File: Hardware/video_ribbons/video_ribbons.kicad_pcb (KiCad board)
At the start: 4 copper layers, 124.5 x 99.1 mm, 82 parts, among them J1 Conn_Coaxial_Sleeve_Pin2Tip, J2 Conn_01x02, J5 Conn_02x08_Odd_Even, J6 Conn_02x04_Odd_Even, J7 Conn_02x08_Odd_Even, U1 74HC138, U10 74HC161, U11 74HC161, U12 74HC30, U13 74HC08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

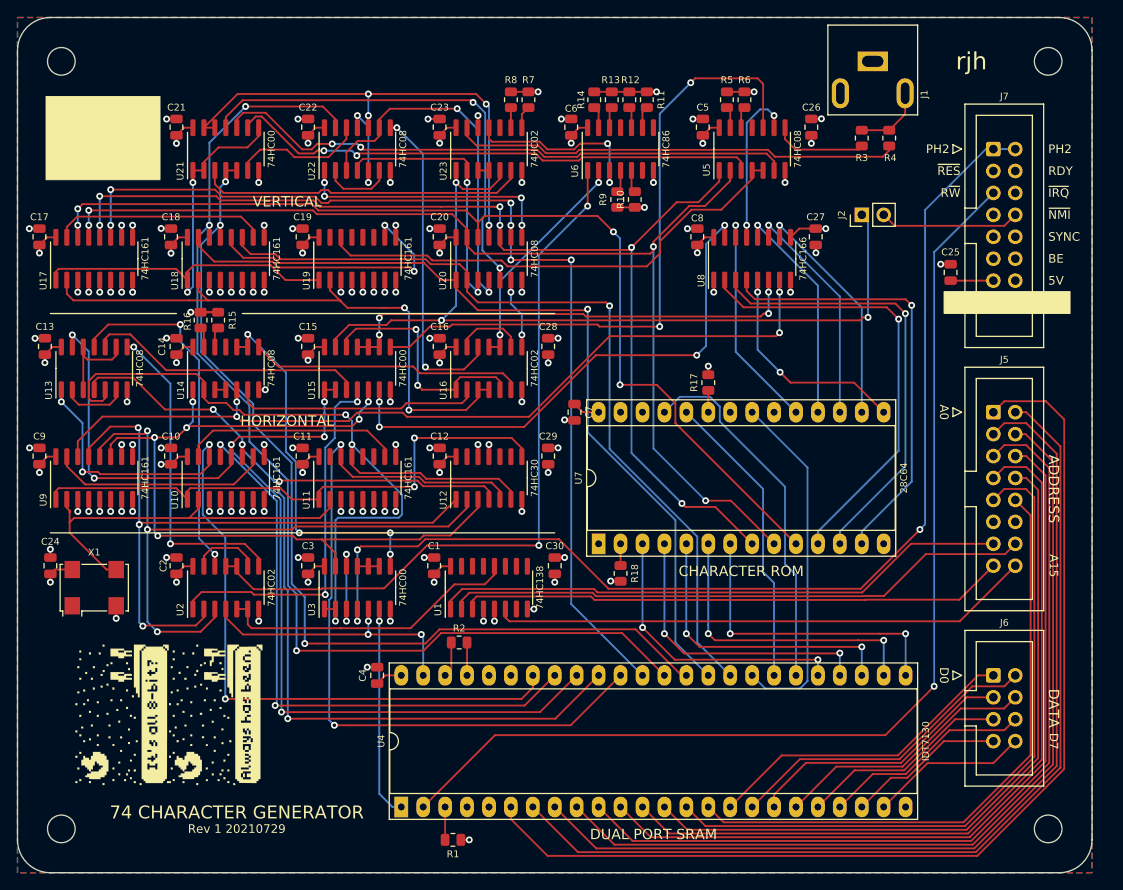
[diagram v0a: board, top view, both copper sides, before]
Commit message: Fix video clear line
Resolves #5.
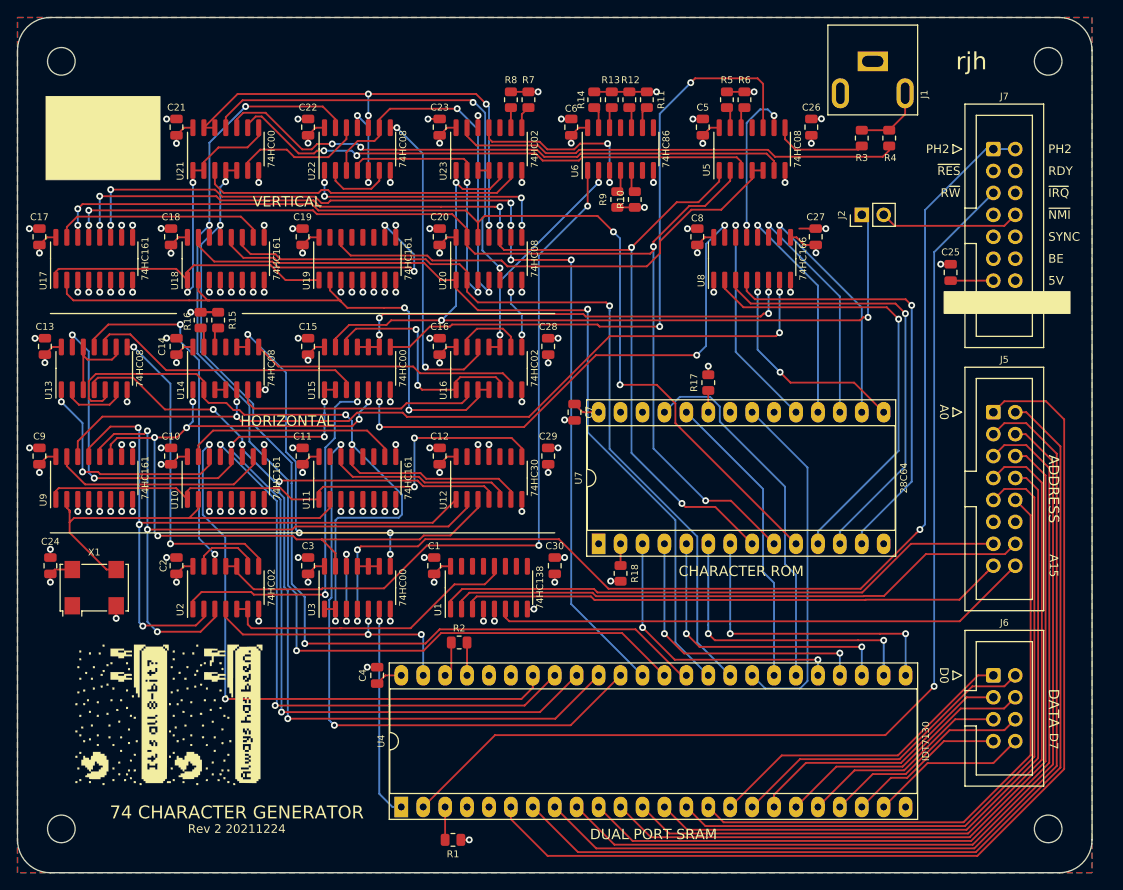
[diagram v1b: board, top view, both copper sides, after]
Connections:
- U8 pad 9: GND -> +5V
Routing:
- net +5V: track 114.5 -> 117.8 mm
- net GND: track 135.7 -> 134.2 mm
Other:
- board text added: "Rev 2 20211224"
- board text removed: "Rev 1 20210729"
